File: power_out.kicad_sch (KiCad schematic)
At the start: 62 parts, among them Q501 BTN8962TA, Q502 BTN8962TA, U501 BTT6200-4ESA

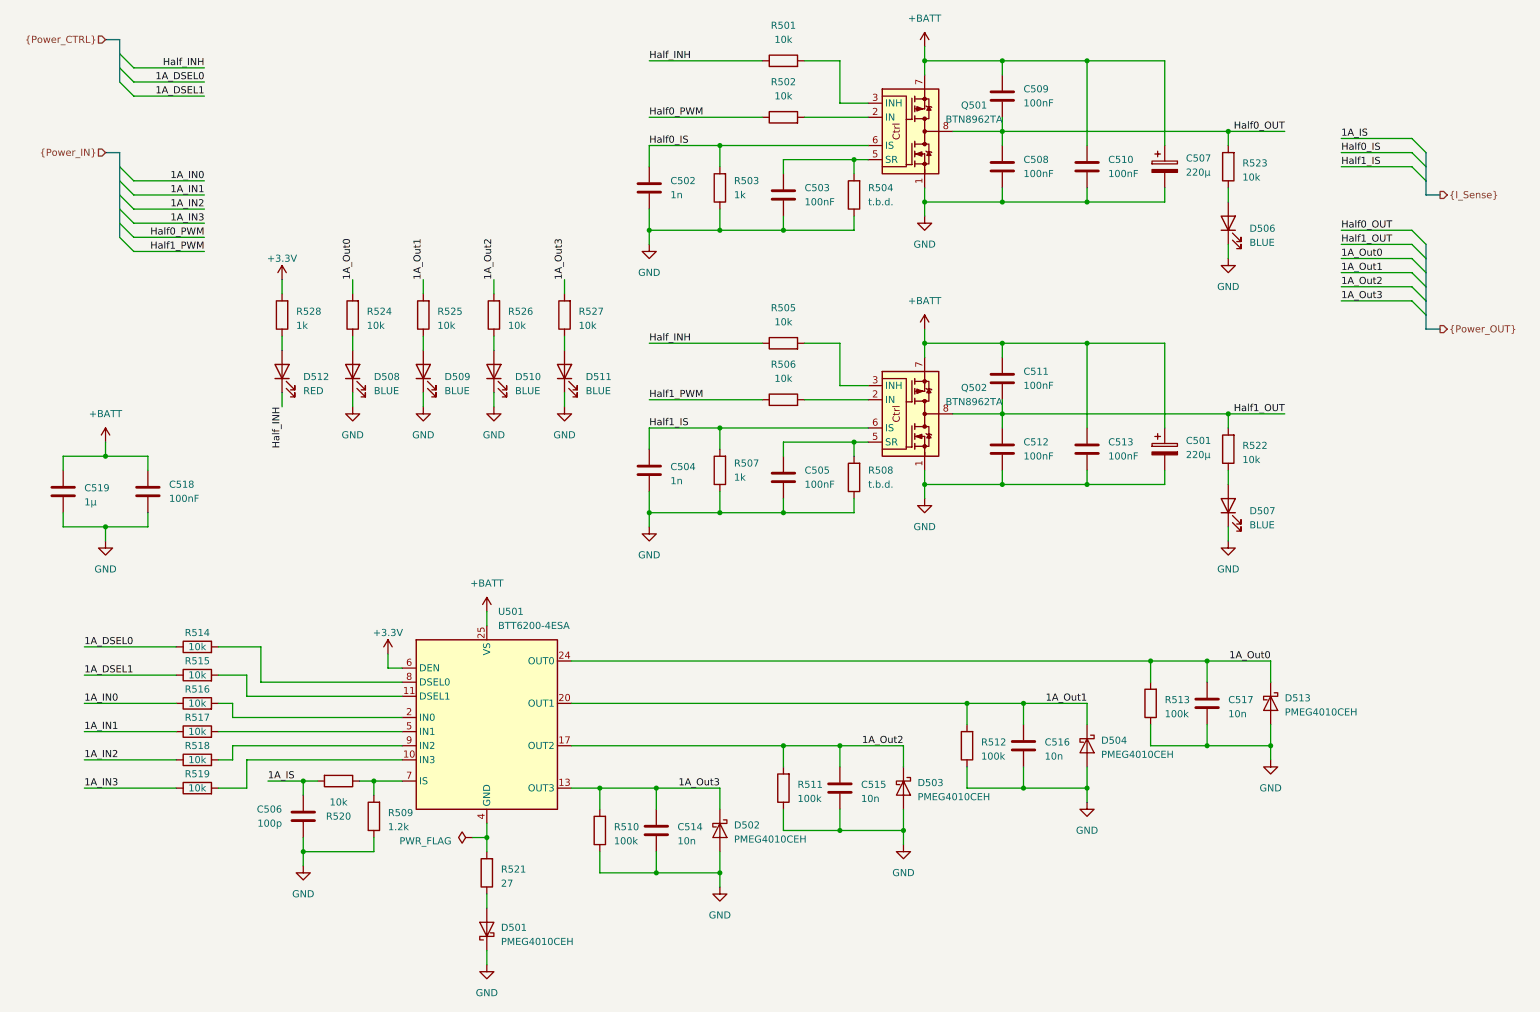
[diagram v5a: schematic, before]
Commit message: hierarchical sheets for digital I/O and replaced power supply jumpers with relays
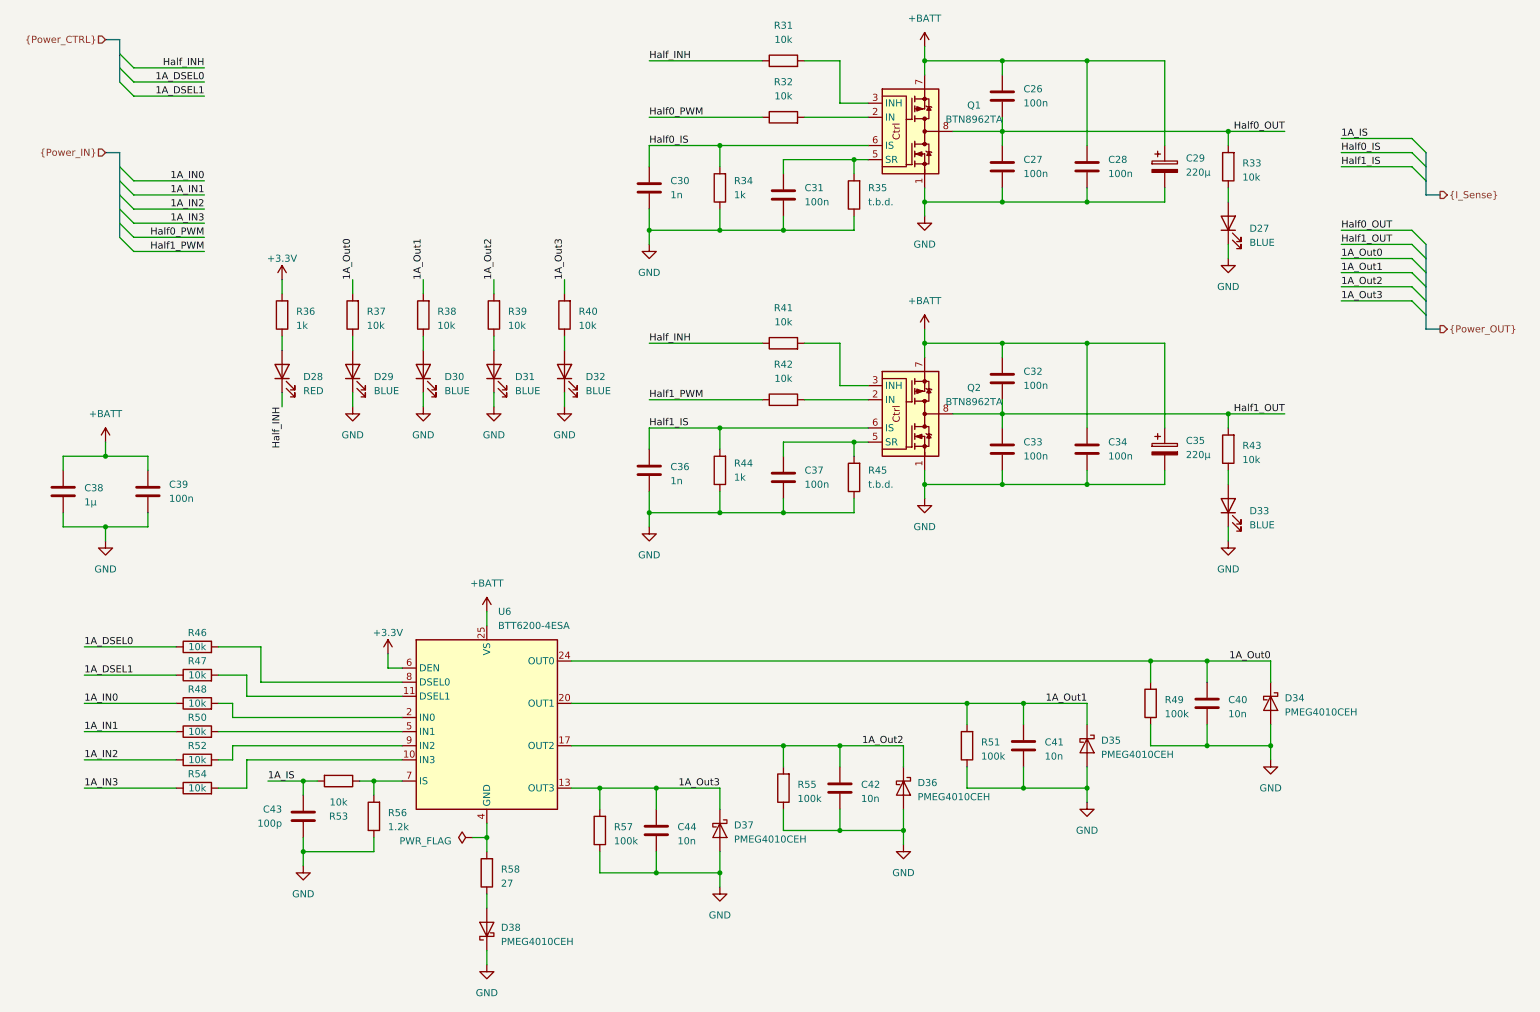
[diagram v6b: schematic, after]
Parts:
- C26: renamed from C509; value 100nF -> 100n
- C27: renamed from C508; value 100nF -> 100n
- C28: renamed from C510; value 100nF -> 100n
- C31: renamed from C503; value 100nF -> 100n
- C32: renamed from C511; value 100nF -> 100n
- C33: renamed from C512; value 100nF -> 100n
- C34: renamed from C513; value 100nF -> 100n
- C37: renamed from C505; value 100nF -> 100n
- C39: renamed from C518; value 100nF -> 100n
- renumbered C507 to C29, C502 to C30, C501 to C35, C504 to C36, C519 to C38, C517 to C40, C516 to C41, C515 to C42, C506 to C43, C514 to C44, D506 to D27, D512 to D28, D508 to D29, D509 to D30, D510 to D31, D511 to D32, D507 to D33, D513 to D34, D504 to D35, D503 to D36, D502 to D37, D501 to D38, Q501 to Q1, Q502 to Q2, R501 to R31, R502 to R32, R523 to R33, R503 to R34, R504 to R35, R528 to R36, R524 to R37, R525 to R38, R526 to R39, R527 to R40, R505 to R41, R506 to R42, R522 to R43, R507 to R44, R508 to R45, R514 to R46, R515 to R47, R516 to R48, R513 to R49, R517 to R50, R512 to R51, R518 to R52, R520 to R53, R519 to R54, R511 to R55, R509 to R56, R510 to R57, R521 to R58, U501 to U6
